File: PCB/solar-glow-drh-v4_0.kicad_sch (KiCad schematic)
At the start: 67 parts, among them J1 UPDI hdr, Q2 BSS138LT1G, SW2 LED master, U1 AVR64EA28 (VQFN28), U3 ADXL367, U5 NT3H2211, U6 TPS22917, U7 MB85RC512TY, U8 AEM10300, U9 TPS7A0233 (SOT23-5*)

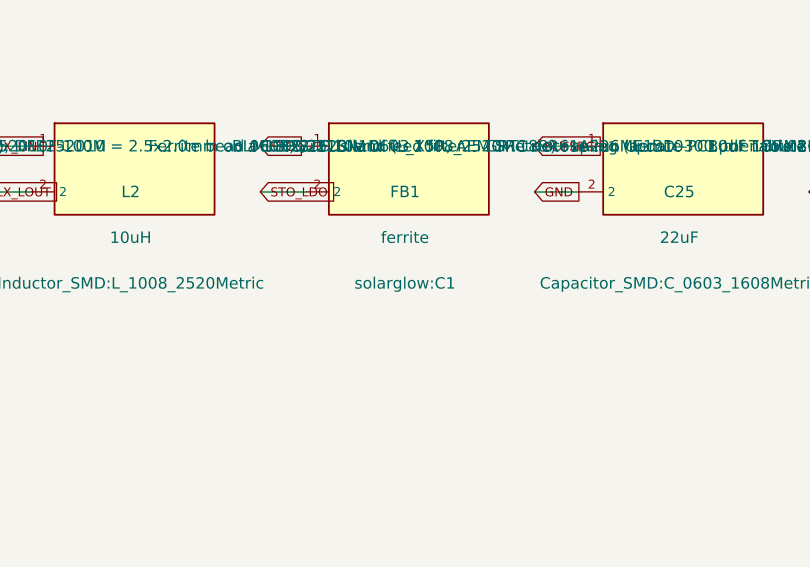
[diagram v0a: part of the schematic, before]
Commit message: FB1: point the schematic at the 0603 land, and add a check that reads the BOM
The 0603 ferrite was a deliberate choice that never reached the copper. It is
recorded in THREE places -- design-notes L157 ("a 0603 ferrite FB1"), the BOM
(BLM18PG221SN1D; Murata BLM18 = 1608 metric = 0603), and the schematic symbol's
own Value ("ferrite *0603") and Description ("Ferrite bead 0603"). The only
field never updated was the Footprint, so schematic AND board both still said
solarglow:C1 -- pads 0.59x0.66 at pitch 1.02, the 0402 land shared with
C1/C24/C29/R17/R18.

The schematic now names Inductor_SMD:L_0603_1608Metric, on both the placed
instance and the cached lib_symbols copy. The other 17 solarglow:C1 references
are untouched. Drawing the 0603 land on the board is a manual KiCad job: the
pads grow 0.59 -> 0.9 wide and the pitch opens 1.02 -> 1.55, so clearance to
its neighbours has to be re-checked.

That deliberately leaves TWO RED GATES until the land is drawn. Both name the
work precisely and clear themselves when it is done:
  drc --schematic-parity -> footprint_symbol_mismatch on FB1
  check_consistency [4]   -> FB1 orders 0603, land is 0402

NEW CHECK. check_consistency.py gains [4] PACKAGE FIT: the package the BOM
orders must match the land the board draws. This exists because nothing in the
toolchain caught FB1 -- KiCad's schematic parity only compares the schematic to
the board, and those two agreed with each other while both were wrong. The BOM
master was the only copy that was right, and no check read it.

Implementation notes worth keeping: the package cell is located by CONTENT, not
by column index, because some BOM rows carry a leading empty cell and a fixed
index lands on the value column instead -- that bug alone limited the first cut
to 15 of 32 comparable parts. Coverage is now 24 of 40 two-pad parts, and the
16 it cannot speak for are PRINTED rather than silently dropped, per this
file's own rule that a checker which quietly ignores parts is worse than n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
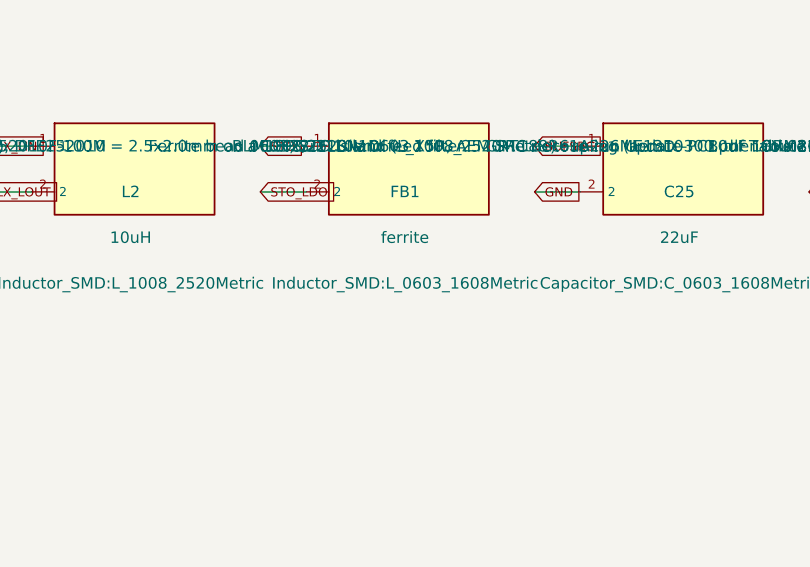
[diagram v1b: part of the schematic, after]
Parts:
- FB1: footprint solarglow:C1 -> Inductor_SMD:L_0603_1608Metric
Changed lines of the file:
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@@
 			)
 		)
-		(property "Footprint" "solarglow:C1"
+		(property "Footprint" "Inductor_SMD:L_0603_1608Metric"
 			(at 562.18 387.35 0)
 			(show_name no)

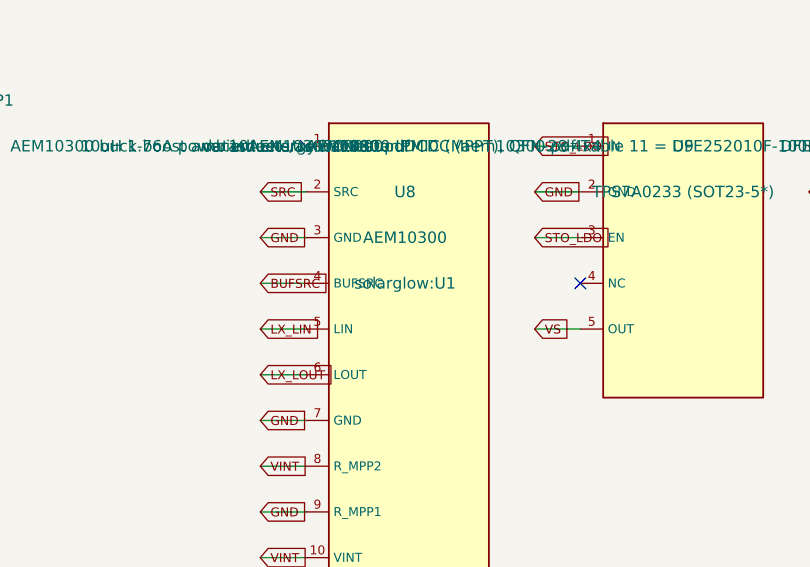
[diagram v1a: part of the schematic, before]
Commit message: enclosure: drop the U7 relief pocket; give U8 its own footprint; close out J1
Three decisions, all now reflected in the sources rather than just the docs.

1. NO RELIEF POCKET. The cavity floor is a true uniform 1.00 mm.

Removed by ARITHMETIC, not deletion: U7_H is corrected 1.75 -> 0.90 (the v4
board's DFN-8, per U7_DFN8.kicad_mod descr / RAMXEED DS501-00087-1v0-E p.21),
so U7_POCKET = max(0, U7_H - cap_H) evaluates to 0 and the generator's existing
`if U7_POCKET > 0` guard skips the cut. The mechanism stays available for the
next part that genuinely needs local relief.

Verified on the regenerated solid rather than assumed: volume 6524.4817 ->
6526.5447 mm^3, +2.0631 back, against a nominal pocket of 7.8 x 5.4 x 0.05 =
2.1060 -- the 0.043 difference is exactly the R1.0 corner fillets. Bounding box
unchanged at 52.700 x 90.800 x 3.550. STEP and STL regenerated.

Two blockers stopped the generator running at all, both the same bug class -- a
path that only ever existed on one machine:
  - OUT was hardcoded to /mnt/user-data/outputs/, so the "source of truth"
    generator could not write its own STEP. Now defaults beside the script.
  - The maker-text fonts pointed at /home/claude/fonts/. Those glyphs are cut
    into the titanium, so the font is part of the deliverable and NOT
    substitutable. JetBrains Mono is vendored in enclosure/fonts/ under SIL OFL
    1.1 with the licence bundled as the OFL requires; MAKER_FONT_DIR overrides,
    and a missing font now fails loudly instead of mid-build.

The 2D drawing is NOT regenerated -- its Detail B still shows the pocket. The
STEP governs so the part is correct, but the PDF is what the shop reads, so the
README now says to state it on the order, and it is tracked as a follow-up.

2. U8 GETS ITS OWN FOOTPRINT. solarglow:U8_QFN28, written from U8's actual board
land and validated by loading it back through KiCad: 29 pads, 14 x 0.8 x 0.2,
14 x 0.2 x 0.8, EP 2.30 x 2.30, 4.000 pad-centre span. Board lib_id and both
schema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
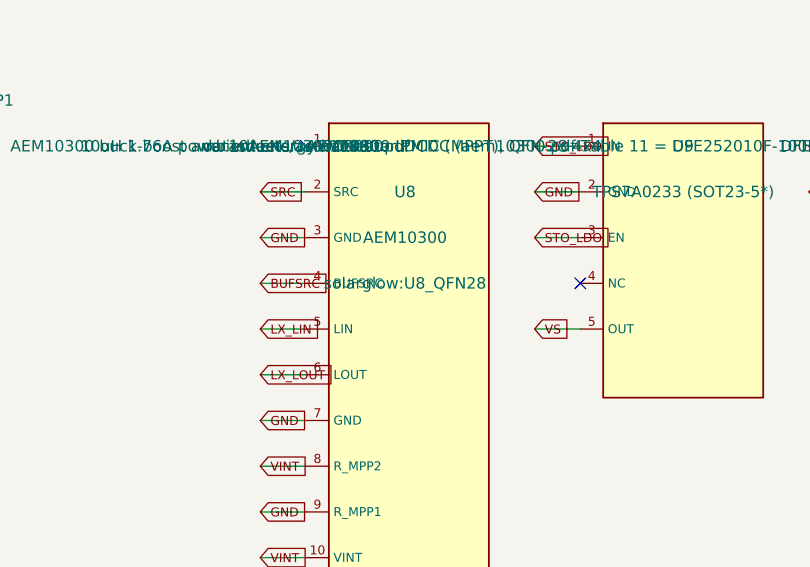
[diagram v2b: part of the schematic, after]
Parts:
- U8: footprint solarglow:U1 -> solarglow:U8_QFN28
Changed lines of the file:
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@@
 			)
 		)
-		(property "Footprint" "solarglow:U1"
+		(property "Footprint" "solarglow:U8_QFN28"
 			(at 470.74 387.35 0)
 			(show_name no)

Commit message: SCH: remove SJ1, and make DRC ERROR while it is still on the board
Completes the SJ1 lifecycle from the schematic end and turns the leftover into a
build failure instead of a note somebody has to remember.

WHAT WAS REMOVED from the .kicad_sch -- six blocks, a self-contained island:
the SJ1 symbol instance; its two stub wires (410.21,160.02)->(405.13,160.02) and
(410.21,165.1)->(405.13,165.1); the two global_labels those stubs landed on (VS
and VDDIO2); and the solarglow:SJ1 lib_symbol. Nothing else touched it -- checked
for junctions, other wires, power symbols and neighbouring pins at all four
endpoints first. 400,716 -> 396,212 bytes, LF endings preserved (this file is LF
while the .kicad_pcb is CRLF; both verified after writing).

U1's Description said "pin 10 (VDDIO2->PD0: SJ1 now DNP)". Rewritten in BOTH
files to say pin 10 is PD0/AIN0 with no MVIO, citing DS40002443A Table 3-1, and
that the strap is removed -- so the parity report carries the one real difference
rather than two.

THE TRIPWIRE. extra_footprint raised warning -> error in .kicad_pro. Safe to
raise rather than blanket: DRC reported 0 footprint errors before this change, so
SJ1 is the ONLY extra footprint -- the board-only parts (MH1-4, MP1-4, TC1) carry
the board_only attribute and do not trip it. Without the bump the finding would
have been one line inside a 217-warning report.

CI IS NOW RED ON PURPOSE and stays red until the board is synced:
  check_consistency -> "on the BOARD but not in the schematic (a sync will
                        DELETE these): SJ1"
  kicad-cli drc      -> "[extra_footprint] ... error ...
                        @(13.3000 mm, 46.0000 mm): Footprint SJ1"
Clear it with Update PCB from Schematic, then Cleanup Tracks & Vias -> remove
dangling, which is also why the copper half was left to KiCad: on VDDIO2 SJ1 is a
pure spur, but on VS the run through (13.16,45.37)->(10.89,47.10) reads as a
through-route past the pad, and which segments were only ever SJ1's is a
connectivi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
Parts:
- removed SJ1: DNP (was 0R VDDIO2 tie), solarglow:SJ1, symbol solarglow:SJ1
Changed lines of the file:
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@@
 		)
 	)
-	(wire
-		(pts
-			(xy 410.21 165.1) (xy 405.13 165.1)
-		)
-		(stroke
-			(width 0)
-			(type default)
-		)
-	)
-	(wire
+		(wire
 		(pts
 			(xy 734.06 377.19) (xy 728.98 377.19)
@@
 		)
 	)
-	(wire
-		(pts
-			(xy 410.21 160.02) (xy 405.13 160.02)
-		)
-		(stroke
-			(width 0)
-			(type default)
-		)
-	)
-	(wire
+		(wire
 		(pts
 			(xy 279.4 160.02) (xy 274.32 160.02)
@@
 		)
 	)
-	(global_label "VS"
-		(shape bidirectional)
-		(at 405.13 160.02 0)
-		(effects
-			(font
-				(size 1 1)
-			)
-		)
-		(property "Intersheetrefs" "${INTERSHEET_REFS}"
-			(at 405.13 160.02 0)
-			(hide yes)
-			(show_name no)
-			(do_not_autoplace no)
-			(effects
-				(font
-					(size 1.27 1.27)
-				)
-			)
-		)
-	)
-	(global_label "SCL"
+		(global_label "SCL"
 		(shape bidirectional)
 		(at 204.47 78.74 0)
@@
 		)
 	)
-	(global_label "VDDIO2"
-		(shape bidirectional)
-		(at 405.13 165.1 0)
-		(effects
-			(font
-				(size 1 1)
-			)
-		)
-		(property "Intersheetrefs" "${INTERSHEET_REFS}"
-			(at 405.13 165.1 0)
-			(hide yes)
-			(show_name no)
-			(do_not_autoplace no)
-			(effects
-				(font
-					(size 1.27 1.27)
-				)
-			)
-		)
-	)
-	(global_label "GND"
+		(global_label "GND"
 		(shape bidirectional)
 		(at 680.72 74.93 0)
@@
 		)
 	)
-	(symbol
-		(lib_id "solarglow:SJ1")
-		(at 410.21 160.02 0)
-		(unit 1)
-		(body_style 1)
-		(exclude_from_sim no)
-		(in_bom yes)
-		(on_board yes)
-		(in_pos_files yes)
-		(dnp yes)
-		(property "Reference" "SJ1"
-			(at 421.21 165.1 0)
-			(show_name no)
-			(do_not_autoplace no)
-			(effects
-				(font
-					(size 1.27 1.27)
-				)
-			)
-		)
-		(property "Value" "DNP (was 0R VDDIO2 tie)"
-			(at 421.21 170.18 0)
-			(show_name no)
-			(do_not_autoplace no)
-			(effects
-				(font
-					(size 1.27 1.27)
-				)
-			)
-		)
-		(property "Footprint" "solarglow:SJ1"
-			(at 421.21 175.26 0)
-			(show_name no)
-			(do_not_autoplace no)
-			(effects
-				(font
-					(size 1.27 1.27)
-				)
-			)
-		)
-		(property "Datasheet" ""
-			(at 410.21 160.02 0)
-			(show_name no)
-			(do_not_autoplace no)
-			(effects
-				(font
-					(size 1.27 1.27)
-				)
-			)
-		)
-		(property "Description" "DNP for the AVR-EA U1: pin 10 is PD0 (GPIO), not VDDIO2 - leave unbridged so PD0 floats (firmware inits it input-disabled). Was the 0R MVIO tie for the DD28."
-			(at 410.21 160.02 0)
-			(show_name no)
-			(do_not_autoplace no)
-			(effects
-				(font
-					(size 1.27 1.27)
-				)
-			)
-		)
-		(property "MPN" "(DNP - not ordered)"
-			(at 410.21 160.02 0)
-			(show_name no)
-			(do_not_autoplace no)
-			(effects
-				(font
-					(size 1.27 1.27)
-				)
-			)
-		)
-		(property "Supplier" "DigiKey"
-			(at 459.74 372.11 0)
-			(hide yes)
-			(show_name no)
-			(do_not_autoplace no)
-			(effects
-				(font
-					(size 1.27 1.27)
-				)
-			)
-		)
-		(property "Supplier P/N" ""
-			(at 459.74 372.11 0)
-			(hide yes)
-			(show_name no)
-			(do_not_autoplace no)
-			(effects
-				(font
-					(size 1.27 1.27)
-				)
-			)
-		)
-		(pin "1"
-		)
-		(pin "2"
-		)
-		(instances
-			(project "solar-glow-drh-v4_0"
-				(path "/bf17630f-b49b-49a7-9335-83fa0a7a44d0"
-					(reference "SJ1")
-					(unit 1)
-				)
-			)
-		)
-	)
-	(symbol
+		(symbol
 		(lib_id "solarglow:U8")
 		(at 459.74 372.11 0)
@@
 			)
 		)
-		(property "Description" "MCU - 8-bit AVR-EA (PWM, I2C, charge/sleep logic); EXTENDED -40..125C. Diff 12-bit ADC+PGA, 512B EEPROM, 80nA base sleep. Pin-compatible with the DD28 copper except pin 10 (VDDIO2->PD0: SJ1 now DNP). FIRMWARE PORT REQUIRED - see TODO."
+		(property "Description" "MCU - 8-bit AVR-EA (PWM, I2C, charge/sleep logic); EXTENDED -40..125C. Diff 12-bit ADC+PGA, 512B EEPROM, 80nA base sleep. Pin-compatible with the DD28 copper except pin 10, which is PD0/AIN0 on the EA, not VDDIO2 (no MVIO: DS40002443A Table 3-1). The DD-era SJ1 strap is REMOVED from this schematic - bridging it would have tied a GPIO to VS. FIRMWARE PORT REQUIRED - see TODO."
 			(at 209.55 38.1 0)
 			(show_name no)

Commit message: SCH: C9 -> 0805 Johanson S-series, and make DRC ERROR on the stale 0402 land
Same pattern as SJ1: change the schematic, and let the tooling demand the board
edit instead of trusting anyone to remember it.

SCHEMATIC. C9's Footprint property goes solarglow:C9 -> Capacitor_SMD:
C_0805_2012Metric, which is the stock land C26/C27 already use, so this
introduces no new library dependency. MPN (DNP) -> QSCT251Q820G1GV001E, plus
Supplier / Supplier P/N fields matching C26's shape. Description rewritten to
name the part and say what DNP means here -- hand-fit on the bench to land
resonance at 13.56 MHz, U5 carrying ~50 pF internally, 82 pF a STARTING POINT to
be trimmed 68-100 -- because "DNP" alone reads as "unused" and this is the one
DNP part that definitely gets fitted.

The (dnp yes) attribute is untouched: DNP-ness lives there, not in the MPN
string, so naming the real part does not put it on the assembly BOM.

THE TRIPWIRE. footprint_symbol_mismatch raised warning -> error. Targeted rather
than blanket: C9 is its only instance in the whole report. DRC now says

  [footprint_symbol_mismatch]: solarglow:C9 doesn't match footprint given by
  symbol (Capacitor_SMD:C_0805_2012Metric)
      Local override; error
      @(35.6600 mm, 39.1400 mm): Footprint C9

footprint_symbol_field_mismatch was deliberately LEFT at warning. It fires on any
text difference -- Description, MPN, Datasheet -- which is documentation drift. A
wrong footprint is a manufacturing fault. Only the second deserves to stop a
build.

Two intentional errors are now armed on this board, both clearing with one KiCad
session: SJ1 (extra_footprint) and C9 (footprint_symbol_mismatch).

VERIFIED:
  ERC        3 -> 3 violations, identical set (pre-existing excluded warnings on
             BTN/PC0/PC1). None introduced.
  netlist    C9 carries footprint Capacitor_SMD:C_0805_2012Metric, MPN
             QSCT251Q820G1GV001E and both supplier fields.
  DRC        rule mix otherwise unchanged; solder_mask_bridge 202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
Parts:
- C9: footprint solarglow:C9 -> Capacitor_SMD:C_0805_2012Metric; MPN (DNP) -> QSCT251Q820G1GV001E; Supplier (none) -> DigiKey; Supplier P/N (none) -> 712-QSCT251Q820G1GV001ETR-ND
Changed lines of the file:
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@@
 			)
 		)
-		(property "Footprint" "solarglow:C9"
+		(property "Footprint" "Capacitor_SMD:C_0805_2012Metric"
 			(at 571.5 129.54 0)
 			(hide yes)
@@
 			)
 		)
-		(property "Description" "NFC antenna trim - DNP (chip internal ~50 pF)"
+		(property "Description" "NFC tank trim, 0805 high-Q C0G +/-2% (Johanson S-series). DNP at assembly - hand-fit on the bench to land resonance at 13.56 MHz; U5 carries ~50 pF internally. Value is a STARTING POINT, trim 68-100 pF."
 			(at 560.07 119.38 0)
 			(hide yes)
@@
 			)
 		)
-		(property "MPN" "(DNP)"
+		(property "MPN" "QSCT251Q820G1GV001E"
 			(at 560.07 119.38 0)
 			(hide yes)
+			(show_name no)
+			(do_not_autoplace no)
+			(effects
+				(font
+					(size 1.27 1.27)
+				)
+			)
+		)
+		(property "Supplier" "DigiKey"
+			(at 560.07 119.38 0)
+			(hide yes)
+			(show_name no)
+			(do_not_autoplace no)
+			(effects
+				(font
+					(size 1.27 1.27)
+				)
+			)
+		)
+		(property "Supplier P/N" "712-QSCT251Q820G1GV001ETR-ND"
+			(at 560.07 119.38 0)
+			(hide yes)
